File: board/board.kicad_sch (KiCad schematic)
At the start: 5 parts, among them J1 022_battery_cells, J2 003_power

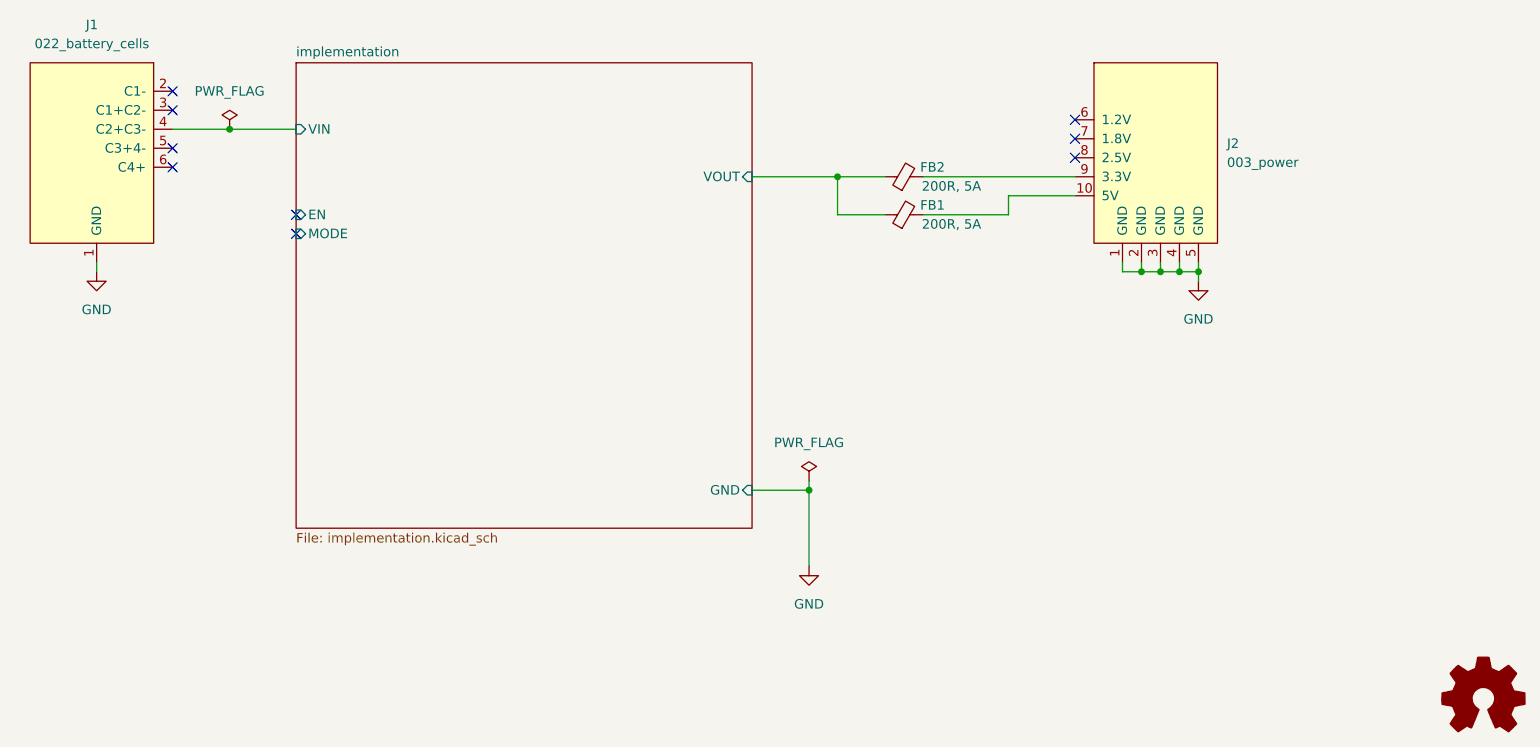
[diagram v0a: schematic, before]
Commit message: reduced ground pins to be compatable with more connector types
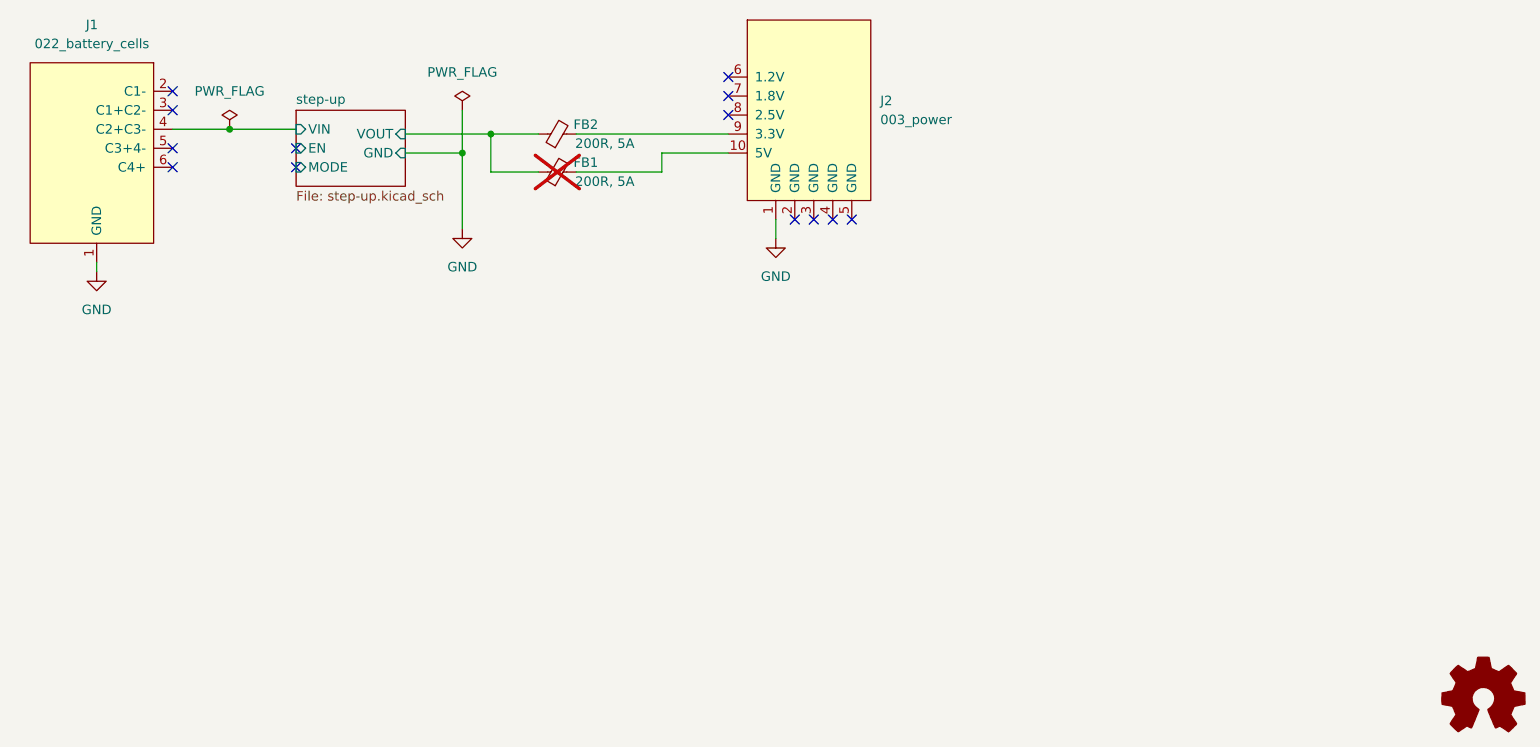
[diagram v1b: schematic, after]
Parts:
- FB1: now not fitted
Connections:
- net GND: no longer J2.2 (GND), J2.3 (GND), J2.4 (GND), J2.5 (GND)
- no-connect marks 9 -> 13
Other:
- sheet implementation renamed step-up
- sheet step-up: file implementation.kicad_sch -> step-up.kicad_sch
- moved on the sheet: FB2, J2
